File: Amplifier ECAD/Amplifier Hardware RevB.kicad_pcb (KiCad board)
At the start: 2 copper layers, 143 x 111 mm, 129 parts, among them J1 SJ1-3525N, J2 NMJ6HFD2, J3 NMJ6HFD2, J4 NMJ6HFD2, J5 NMJ6HFD2, J6 NMJ6HFD2, J7 SJ1-3525N, SW1 EC11, SW2 EC11, SW3 EC11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

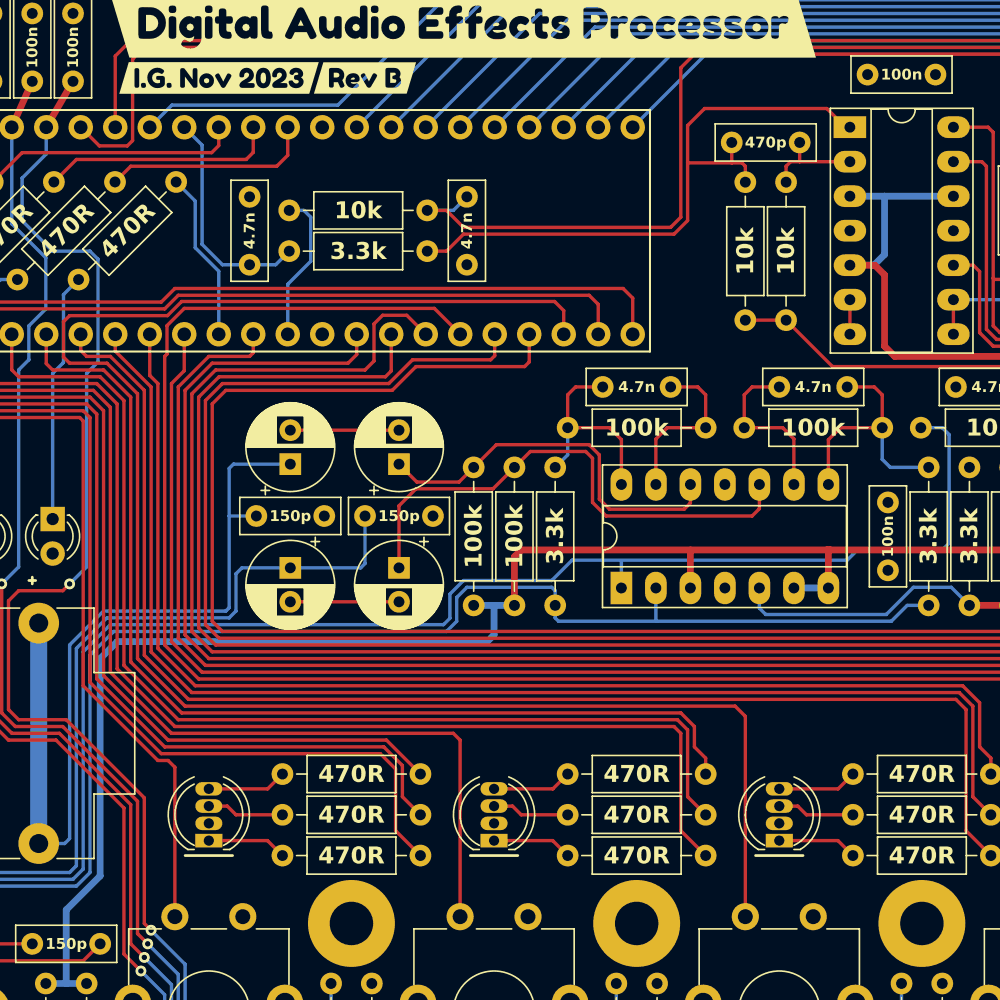
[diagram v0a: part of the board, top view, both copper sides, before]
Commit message: File renaming; updating supplier references
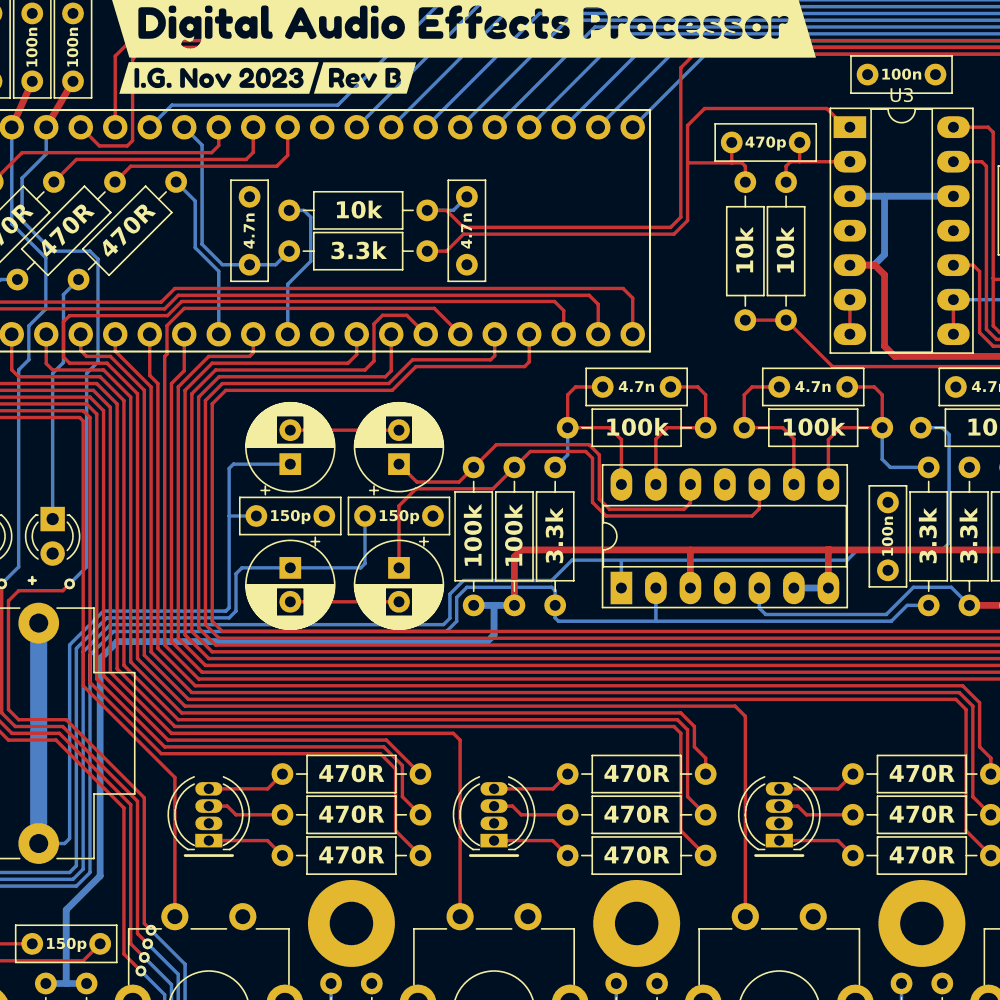
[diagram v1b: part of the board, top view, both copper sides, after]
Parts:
- C1, C10, C16, C17, C18, C19, C2, C3, C4, C7, C8, C9: footprint Custom-RLC:CP_Radial_D6.3mm_H12.5_P2.50mm -> Custom-RLC:CP_KEMET_ESY
- C11, C12, C14, C15, C20, C22, C23, C25: footprint Custom-RLC:C_Disc_L7.2mm_W2.5mm_H6.6mm_P5.00mm_MODIFIED_1 -> Custom-RLC:C_KEMET_C322
- C13, C21, C24, C26, C27, C28, C29, C30, C31, C32, C33, C5, C6: footprint Custom-RLC:C_Disc_L7.2mm_W2.5mm_H6.6mm_P5.00mm_MODIFIED_1 -> Custom-RLC:C_KEMET_C317
- D6, D7, D8: value WHITE -> YELLOW
- H1, H2, H3, H4, H5, H6, H7, H8: value MountingHole_Pad -> M3
- J1, J7: value SJ1-3525N -> 3.5mm TRS

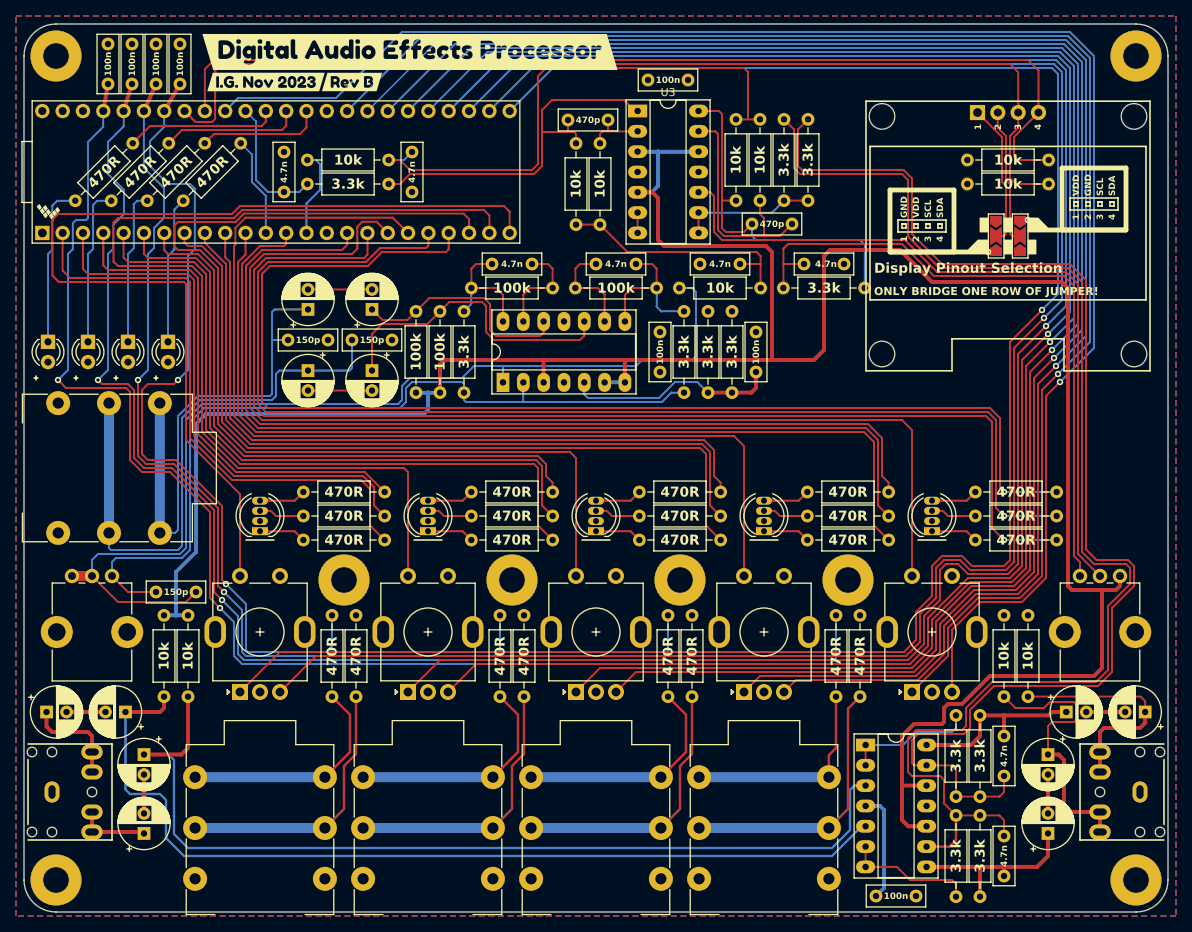
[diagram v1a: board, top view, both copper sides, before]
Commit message: Front and rear panel work; renderings on Fusion360
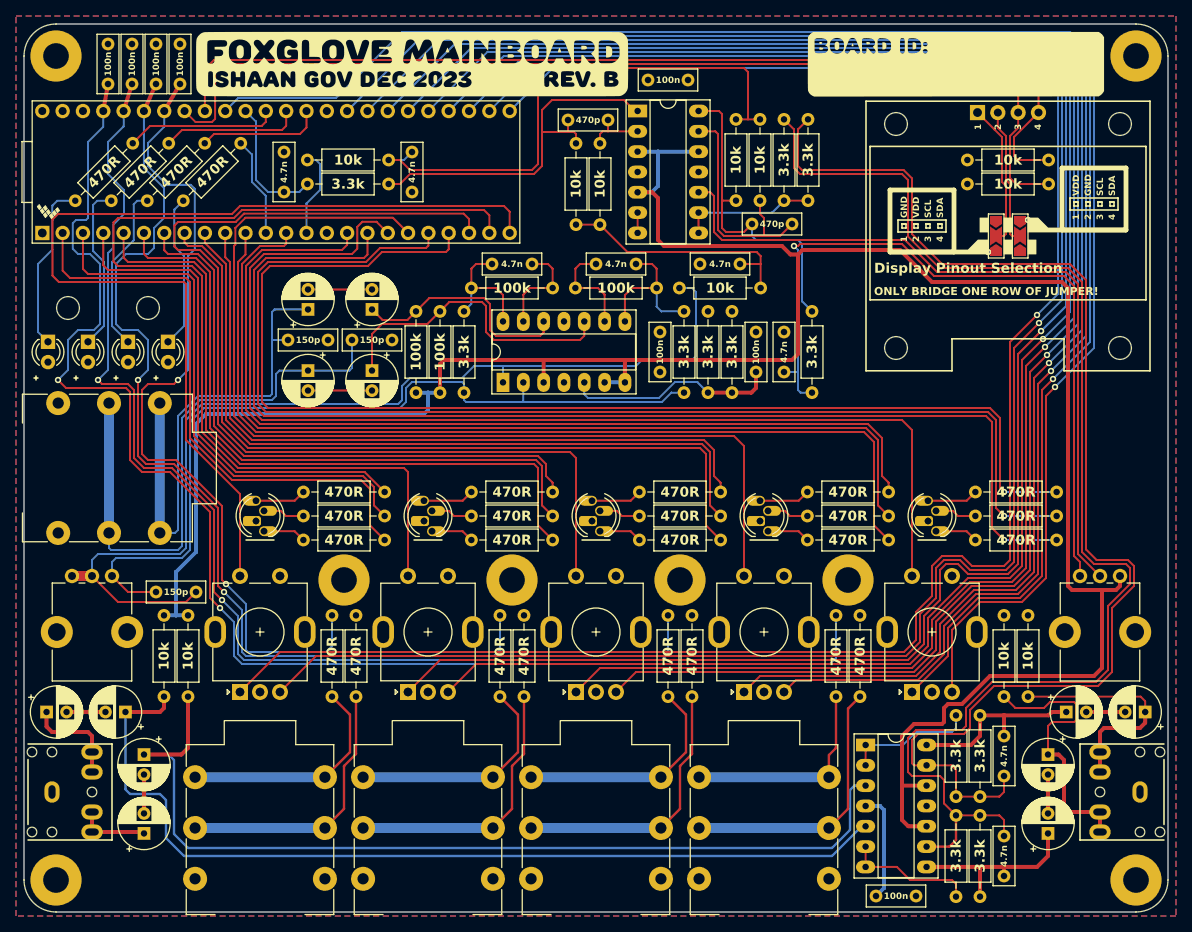
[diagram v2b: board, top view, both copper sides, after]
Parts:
- removed kibuzzard-6562A21D: G***, kibuzzard-6562A21D
- removed kibuzzard-6562A25D: G***, kibuzzard-6562A25D
- removed kibuzzard-65713D98: G***, kibuzzard-65713D98
- added G***: LOGO, LOGO, F.Cu at (129.0, 42.2)
- added G***: LOGO, LOGO, F.Cu at (197.0, 42.2)
- added H10: M2.6, Custom-Mechanical:MountingHole_2.9mm_5.5mm_Ring, F.Cu at (217.5, 77.8)
- added H11: M2.6, Custom-Mechanical:MountingHole_2.9mm_5.5mm_Ring, F.Cu at (189.5, 49.8)
- added H12: M2.6, Custom-Mechanical:MountingHole_2.9mm_5.5mm_Ring, F.Cu at (189.5, 77.8)
- added H13: M2.6, Custom-Mechanical:MountingHole_2.9mm_5.5mm_Ring, F.Cu at (86.0, 72.8)
- added H14: M2.6, Custom-Mechanical:MountingHole_2.9mm_5.5mm_Ring, F.Cu at (96.0, 72.8)
- added H9: M2.6, Custom-Mechanical:MountingHole_2.9mm_5.5mm_Ring, F.Cu at (217.5, 49.8)
- moved C25 13.7 mm to (175.5, 80.8), turned to 90 degrees
- moved R24 7.20 mm to (179.0, 73.2), turned to -90 degrees
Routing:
- net /Reconstruction Filter/EFFECT_RECON: track 82.8 -> 95.7 mm, vias 0 -> 1
- net /BIAS: track 321.3 -> 311.5 mm
- net /Effect Channel 2/EXP_IN: track 118.2 -> 124.3 mm
- net /Effect Channel 4/EXP_IN: track 171.5 -> 176.4 mm
- net Net-(C24-Pad1): track 44.9 -> 40.6 mm
- net Net-(D7-K): track 19.4 -> 21.0 mm
- net Net-(D6-K): track 19.9 -> 21.0 mm
- net Net-(D5-K): track 20.4 -> 21.4 mm
- net Net-(D8-K): track 18.4 -> 19.4 mm
- net Net-(D1-BK): track 5.69 -> 5.19 mm
- net Net-(D9-RK): track 5.88 -> 5.38 mm
- net Net-(D9-GK): track 5.87 -> 6.37 mm
- net Net-(D9-BK): track 5.69 -> 5.19 mm
- net Net-(D4-RK): track 5.88 -> 5.38 mm
- net Net-(D4-GK): track 5.87 -> 6.37 mm
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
